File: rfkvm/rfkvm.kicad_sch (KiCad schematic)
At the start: 18 parts, among them K1 G6SK-2, K2 G6SK-2, Q1 PN2222A, Q2 PN2222A, SW1 SW_Push, SW2 SW_Push, SW3 SW_Push, U2 USB-C Breakout, U3 USB-C Breakout

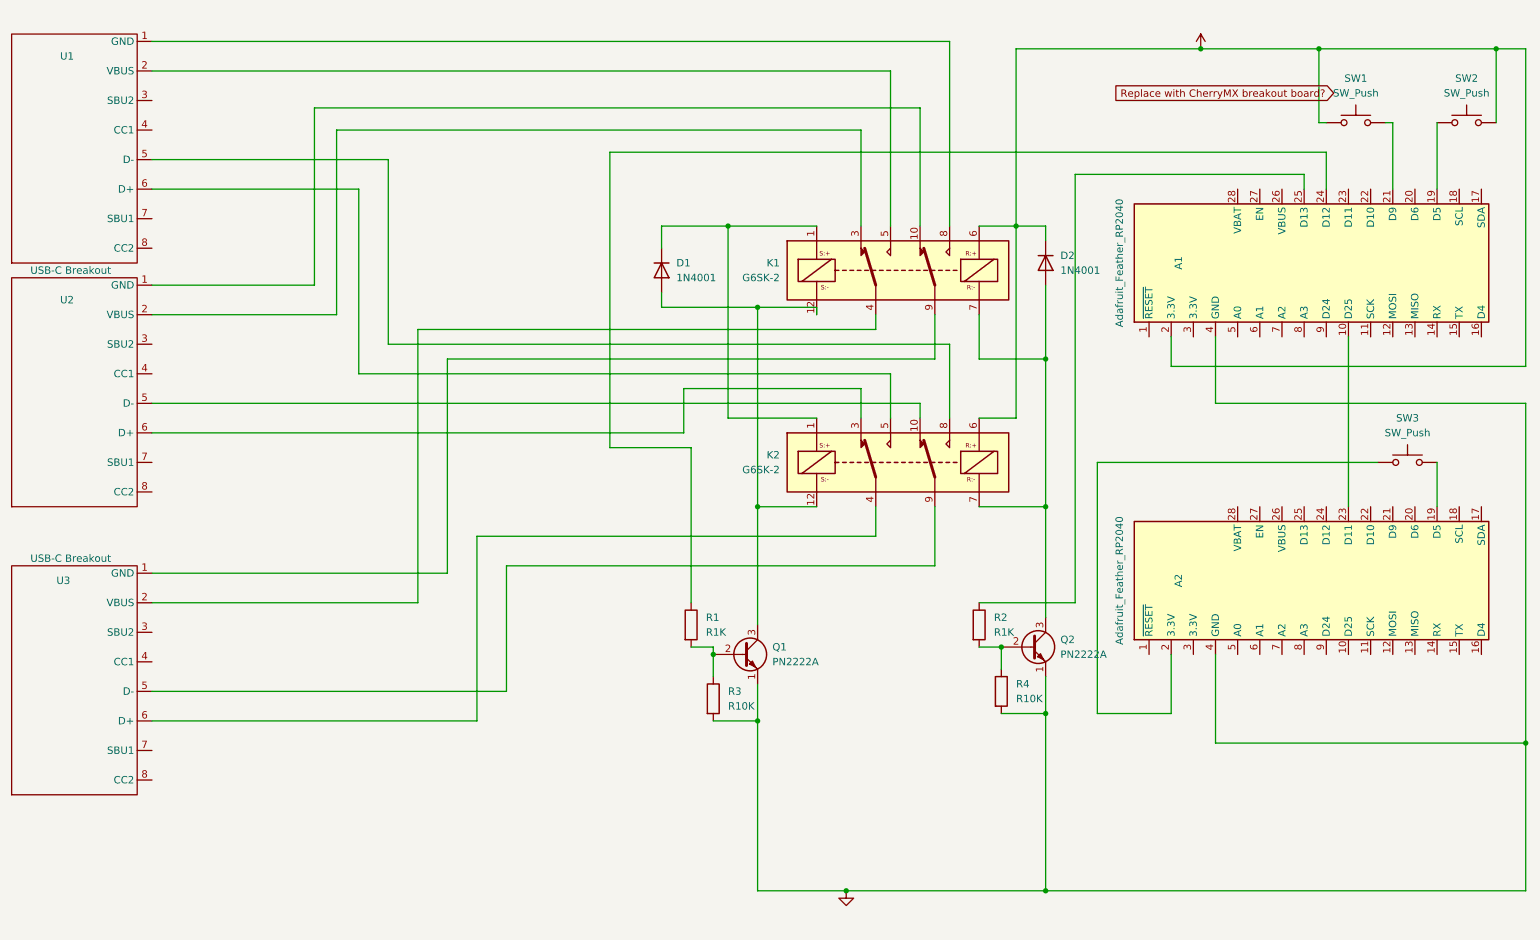
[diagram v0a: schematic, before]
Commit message: Various updates and fixes * Only GND plane, no 3.3v plane, reduces complexity * Added text for version * Added graphics for fun * Fixed some alignments * Might have fixed some unconnected pads
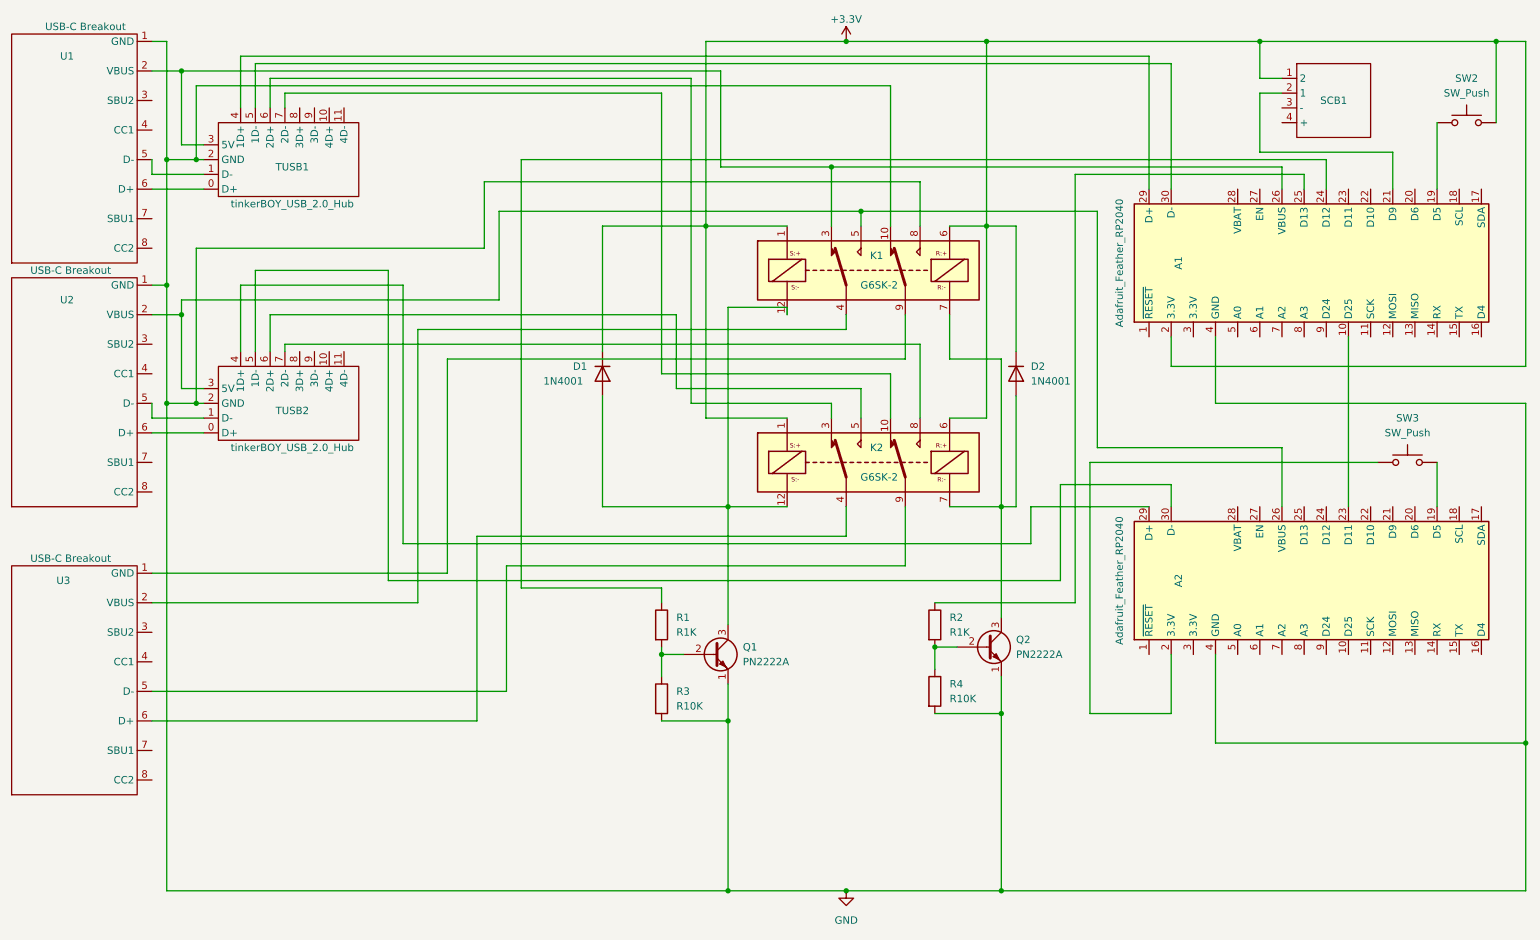
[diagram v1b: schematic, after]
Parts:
- removed SW1: SW_Push, Button_Switch_THT:SW_Tactile_Straight_KSL0Axx1LFTR, symbol Switch:SW_Push
- added SCB1: (no value), symbol SparkFun:Sparkfun_Cherry_MX_Switch_Breakout
- added TUSB1, TUSB2: tinkerBOY_USB_2.0_Hub, tinkerBOY:tinkerBOY USB 2.0 Hub, symbol tinkeyBOY:tinkerBOY_USB_2.0_Hub
- A1, A2: footprint (none) -> Adafruit:Adafruit Feather RP2040
- U1: value (none) -> USB-C Breakout; footprint (none) -> Adafruit:Adafruit 4090 - USB-C Breakout
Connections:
- net +3V3: now also D1.1 (K), K1.1, K2.1, SCB1.1 (2)
- net GND: now also K1.10, K1.8, U1.1 (GND), U2.1 (GND), TUSB1.2 (GND), TUSB2.2 (GND)
- net at U2.2 (VBUS): now also A2.26 (VBUS), K1.5, TUSB2.3 (5V); no longer K1.3
- net at U2.5 (D-): now also TUSB2.1 (D-); no longer K2.10
- net at U2.6 (D+): now also TUSB2.0 (D+); no longer K2.3
- net at A1.21 (D9): now also SCB1.2 (1)
- net at U1.2 (VBUS): now also A1.26 (VBUS), K1.3, TUSB1.3 (5V); no longer K1.5
- net at U1.6 (D+): now also TUSB1.0 (D+); no longer K2.5
- net at U1.5 (D-): now also TUSB1.1 (D-); no longer K2.8
- new net: A2.29 (D+), TUSB2.4 (1D+)
- new net: A2.30 (D-), TUSB2.5 (1D-)
- new net: A1.29 (D+), TUSB1.4 (1D+)
- new net: A1.30 (D-), TUSB1.5 (1D-)
- new net: K2.3, TUSB1.6 (2D+)
- new net: K2.10, TUSB1.7 (2D-)
- new net: K2.5, TUSB2.6 (2D+)
- new net: K2.8, TUSB2.7 (2D-)
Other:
- moved on the sheet: D1, D2, K1, K2, Q1, Q2, R1, R2, R3, R4
